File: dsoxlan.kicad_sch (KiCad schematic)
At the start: 6 parts, among them P1 CNT-RJ45, P2 CONN_02X40

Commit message: Basic upgrade to Kicad 7+
Symbols had to be recreated because they were not part of
original dataset.

Footprint library now needs to end in .pretty

Still many DRC warnings, but the basic result ought to be
the same as before now.
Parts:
- C2: footprint Capacitors_SMD:C_0805_HandSoldering -> Capacitor_SMD:C_0805_2012Metric_Pad1.18x1.45mm_HandSolder
- R1, R2, R3: footprint Resistors_SMD:R_0805_HandSoldering -> Resistor_SMD:R_0805_2012Metric_Pad1.20x1.40mm_HandSolder
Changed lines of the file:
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@@
       (effects (font (size 1.016 1.016)))
     )
-    (property "Footprint" "Resistors_SMD:R_0805_HandSoldering" (at 109.22 96.012 90)
+    (property "Footprint" "Resistor_SMD:R_0805_2012Metric_Pad1.20x1.40mm_HandSolder" (at 109.22 96.012 90)
       (effects (font (size 1.27 1.27)) hide)
     )
@@
       (effects (font (size 1.016 1.016)))
     )
-    (property "Footprint" "Resistors_SMD:R_0805_HandSoldering" (at 109.22 88.392 90)
+    (property "Footprint" "Resistor_SMD:R_0805_2012Metric_Pad1.20x1.40mm_HandSolder" (at 109.22 88.392 90)
       (effects (font (size 1.27 1.27)) hide)
     )
@@
       (effects (font (size 1.016 1.016)) (justify left))
     )
-    (property "Footprint" "Capacitors_SMD:C_0805_HandSoldering" (at 110.1852 71.12 0)
+    (property "Footprint" "Capacitor_SMD:C_0805_2012Metric_Pad1.18x1.45mm_HandSolder" (at 110.1852 71.12 0)
       (effects (font (size 1.27 1.27)) hide)
     )
@@
       (effects (font (size 1.016 1.016)))
     )
-    (property "Footprint" "Resistors_SMD:R_0805_HandSoldering" (at 118.11 71.882 90)
+    (property "Footprint" "Resistor_SMD:R_0805_2012Metric_Pad1.20x1.40mm_HandSolder" (at 118.11 71.882 90)
       (effects (font (size 1.27 1.27)) hide)
     )

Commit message: DSC fixup
Replace all objects by new ones from the current libraries
shipped by Kicad.

This causes a slightly different OSHW (Opensource Hardware)
logo to be used in the PCB.

To maintain schematic parity, all mechanical objects on the
PCB (mounting holes and OSHW logo) have their schematic
counterparts now.
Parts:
- added H101, H102, H103, H104: MountingHole, MountingHole:MountingHole_3.2mm_M3_ISO7380, symbol Mechanical:MountingHole
- added SYM101: Logo_Open_Hardware_Small, Symbol:OSHW-Symbol_6.7x6mm_Copper, symbol Graphic:Logo_Open_Hardware_Small
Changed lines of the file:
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@@
+    )
+  )
+  (symbol (lib_id "Mechanical:MountingHole") (at 83.82 139.7 0) (unit 1)
+    (in_bom yes) (on_board yes) (dnp no) (fields_autoplaced)
+    (property "Reference" "H101" (at 86.36 139.0563 0)
+      (effects (font (size 1.27 1.27)) (justify left))
+    )
+    (property "Value" "MountingHole" (at 86.36 140.9773 0)
+      (effects (font (size 1.27 1.27)) (justify left))
+    )
+    (property "Footprint" "MountingHole:MountingHole_3.2mm_M3_ISO7380" (at 83.82 139.7 0)
+      (effects (font (size 1.27 1.27)) hide)
+    )
+    (property "Datasheet" "~" (at 83.82 139.7 0)
+      (effects (font (size 1.27 1.27)) hide)
+    )
+    (instances
+      (project "dsoxlan"
+        (path "/071cacbe-efce-4cc8-8d6c-a55997c1e3c5"
+          (reference "H101") (unit 1)
+        )
+      )
+    )
+  )
+  (symbol (lib_id "Mechanical:MountingHole") (at 83.82 158.75 0) (unit 1)
+    (in_bom yes) (on_board yes) (dnp no) (fields_autoplaced)
+    (property "Reference" "H104" (at 86.36 158.1063 0)
+      (effects (font (size 1.27 1.27)) (justify left))
+    )
+    (property "Value" "MountingHole" (at 86.36 160.0273 0)
+      (effects (font (size 1.27 1.27)) (justify left))
+    )
+    (property "Footprint" "MountingHole:MountingHole_3.2mm_M3_ISO7380" (at 83.82 158.75 0)
+      (effects (font (size 1.27 1.27)) hide)
+    )
+    (property "Datasheet" "~" (at 83.82 158.75 0)
+      (effects (font (size 1.27 1.27)) hide)
+    )
+    (instances
+      (project "dsoxlan"
+        (path "/071cacbe-efce-4cc8-8d6c-a55997c1e3c5"
+          (reference "H104") (unit 1)
+        )
+      )
+    )
+  )
+  (symbol (lib_id "Mechanical:MountingHole") (at 83.82 146.05 0) (unit 1)
+    (in_bom yes) (on_board yes) (dnp no) (fields_autoplaced)
+    (property "Reference" "H102" (at 86.36 145.4063 0)
+      (effects (font (size 1.27 1.27)) (justify left))
+    )
+    (property "Value" "MountingHole" (at 86.36 147.3273 0)
+      (effects (font (size 1.27 1.27)) (justify left))
+    )
+    (property "Footprint" "MountingHole:MountingHole_3.2mm_M3_ISO7380" (at 83.82 146.05 0)
+      (effects (font (size 1.27 1.27)) hide)
+    )
+    (property "Datasheet" "~" (at 83.82 146.05 0)
+      (effects (font (size 1.27 1.27)) hide)
+    )
+    (instances
+      (project "dsoxlan"
+        (path "/071cacbe-efce-4cc8-8d6c-a55997c1e3c5"
+          (reference "H102") (unit 1)
+        )
+      )
+    )
+  )
+  (symbol (lib_id "Graphic:Logo_Open_Hardware_Small") (at 86.36 175.26 0) (unit 1)
+    (in_bom no) (on_board yes) (dnp no) (fields_autoplaced)
+    (property "Reference" "SYM101" (at 86.36 168.275 0)
+      (effects (font (size 1.27 1.27)) hide)
+    )
+    (property "Value" "Logo_Open_Hardware_Small" (at 86.36 180.975 0)
+      (effects (font (size 1.27 1.27)) hide)
+    )
+    (property "Footprint" "Symbol:OSHW-Symbol_6.7x6mm_Copper" (at 86.36 175.26 0)
+      (effects (font (size 1.27 1.27)) hide)
+    )
+    (property "Datasheet" "~" (at 86.36 175.26 0)
+      (effects (font (size 1.27 1.27)) hide)
+    )
+    (property "Sim.Enable" "0" (at 86.36 175.26 0)
+      (effects (font (size 1.27 1.27)) hide)
+    )
+    (instances
+      (project "dsoxlan"
+        (path "/071cacbe-efce-4cc8-8d6c-a55997c1e3c5"
+          (reference "SYM101") (unit 1)
+        )
+      )
+    )
+  )
+  (symbol (lib_id "Mechanical:MountingHole") (at 83.82 152.4 0) (unit 1)
+    (in_bom yes) (on_board yes) (dnp no) (fields_autoplaced)
+    (property "Reference" "H103" (at 86.36 151.7563 0)
+      (effects (font (size 1.27 1.27)) (justify left))
+    )
+    (property "Value" "MountingHole" (at 86.36 153.6773 0)
+      (effects (font (size 1.27 1.27)) (justify left))
+    )
+    (property "Footprint" "MountingHole:MountingHole_3.2mm_M3_ISO7380" (at 83.82 152.4 0)
+      (effects (font (size 1.27 1.27)) hide)
+    )
+    (property "Datasheet" "~" (at 83.82 152.4 0)
+      (effects (font (size 1.27 1.27)) hide)
+    )
+    (instances
+      (project "dsoxlan"
+        (path "/071cacbe-efce-4cc8-8d6c-a55997c1e3c5"
+          (reference "H103") (unit 1)
+        )
+      )
     )
   )

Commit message: Replace RJ45 jack by Bel Fuse 08B0-1X1T-36-F
The old TE Connectivity device is no longer available.

Found another one that contains similar magnetics and
termination as the TE one.
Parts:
- removed P1: CNT-RJ45, DSOXLAN:ETH-MAGJACK, symbol dsoxlan:CNT-RJ45
- added P1: 08B0-1X1T-36-F, DSOXLAN:08B0-1X1T-36-F, symbol dsoxlan:RJ45-BELFUSE
- R1, R2: value 220R -> 470R
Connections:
- net GND: now also P1.13 (Shield), P1.14 (Shield)
- net LED1: now also P1.7 (D1)
- net LED2: now also P1.9 (D3)
- net RX+: now also P1.2
- net RX-: now also P1.3
- net TX+: now also P1.4
- net TX-: now also P1.5
- net at R1.2: now also P1.8 (D2)
- net at R2.2: now also P1.10 (D4)
- net at C2.2, R3.2: now also P1.1, P1.6
- no-connect marks 67 -> 66
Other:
- note added: "AW 2014-12-18, DL8DTL 2024-05-18"
- note removed: "AW 2014-12-18"
- note removed: "Digi-Key 1419-1021-ND"
- moved on the sheet: R1, R2

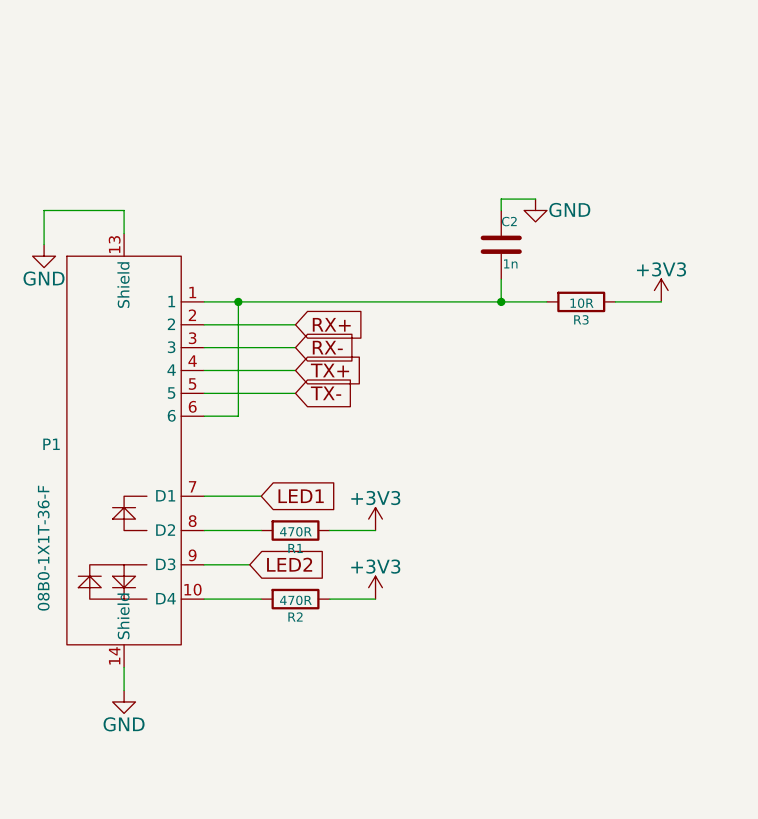
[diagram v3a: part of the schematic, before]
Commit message: Replace RJ45 jack by Würth 7499010121A
This one appears to be readily available at various distributors.

Also add 3D print models for case parts, obtained from

https://www.eevblog.com/forum/projects/diy-dsoxlan-interface-for-keysight-oscilloscopes/msg4323214/#msg4323214

apparently authored by Jay_Diddy_B.

Adapted layout to fit these models.
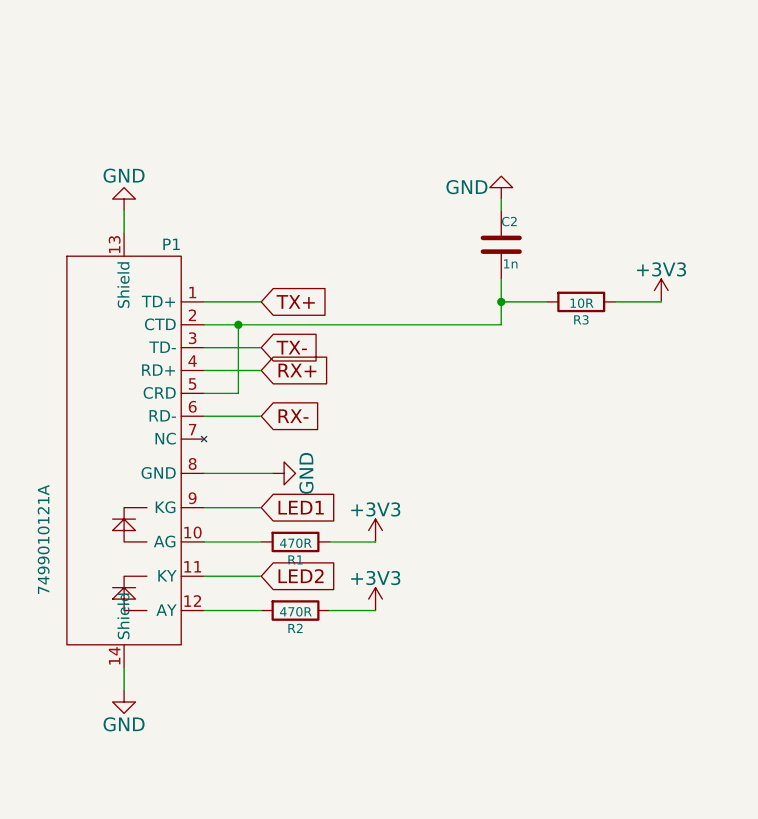
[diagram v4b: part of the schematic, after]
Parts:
- P1: value 08B0-1X1T-36-F -> 7499010121A; footprint DSOXLAN:08B0-1X1T-36-F -> DSOXLAN:WURTH-7499010121A; symbol dsoxlan:RJ45-BELFUSE -> dsoxlan:WÜRTH-7499010121A
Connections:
- net GND: now also P1.8 (GND)
- net LED1: now also P1.9 (KG); no longer P1.7 (D1)
- net LED2: now also P1.11 (KY); no longer P1.9 (D3)
- net RX+: now also P1.4 (RD+); no longer P1.2
- net RX-: now also P1.6 (RD-); no longer P1.3
- net TX+: now also P1.1 (TD+); no longer P1.4
- net TX-: now also P1.3 (TD-); no longer P1.5
- net at R2.2: now also P1.12 (AY); no longer P1.10 (D4)
- net at R1.2: now also P1.10 (AG); no longer P1.8 (D2)
- net at C2.2, R3.2: now also P1.2 (CTD), P1.5 (CRD); no longer P1.1, P1.6
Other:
- moved on the sheet: R1, R2

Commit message: update to kicad9
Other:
- title: (none) -> DSOXLAN
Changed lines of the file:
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@@
 (kicad_sch
-	(version 20231120)
+	(version 20250114)
 	(generator "eeschema")
-	(generator_version "8.0")
+	(generator_version "9.0")
 	(paper "A4")
+	(title_block
+		(title "DSOXLAN")
+	)
+	(text "bottom-side"
+		(exclude_from_sim no)
+		(at 201.93 138.43 0)
+		(effects
+			(font
+				(size 1.524 1.524)
+			)
+			(justify left bottom)
+		)
+	)
+	(text "top-side"
+		(exclude_from_sim no)
+		(at 170.18 34.29 0)
+		(effects
+			(font
+				(size 1.524 1.524)
+			)
+			(justify left bottom)
+		)
+	)
+	(text "left edge of card"
+		(exclude_from_sim no)
+		(at 179.07 139.7 0)
+		(effects
+			(font
+				(size 1.524 1.524)
+			)
+			(justify left bottom)
+		)
+	)
+	(text "DIY DSOXLAN for Agilent DSO-X 2000 and 3000"
+		(exclude_from_sim no)
+		(at 193.04 173.99 0)
+		(effects
+			(font
+				(size 1.524 1.524)
+			)
+			(justify left bottom)
+		)
+	)
+	(text "AW 2014-12-18, DL8DTL 2024-05-18"
+		(exclude_from_sim no)
+		(at 193.04 179.07 0)
+		(effects
+			(font
+				(size 1.524 1.524)
+			)
+			(justify left bottom)
+		)
+	)
+	(text "right edge of card"
+		(exclude_from_sim no)
+		(at 177.8 30.48 0)
+		(effects
+			(font
+				(size 1.524 1.524)
+			)
+			(justify left bottom)
+		)
+	)
+	(text "top-side"
+		(exclude_from_sim no)
+		(at 167.64 137.16 0)
+		(effects
+			(font
+				(size 1.524 1.524)
+			)
+			(justify left bottom)
+		)
+	)
+	(text "bottom-side"
+		(exclude_from_sim no)
+		(at 198.12 34.29 0)
+		(effects
+			(font
+				(size 1.524 1.524)
+			)
+			(justify left bottom)
+		)
+	)
+	(text "notch in card-edge connector"
+		(exclude_from_sim no)
+		(at 200.66 90.17 0)
+		(effects
+			(font
+				(size 1.524 1.524)
+			)
+			(justify left bottom)
+		)
+	)
+	(text "LAN_EN"
+		(exclude_from_sim no)
+		(at 200.66 134.62 0)
+		(effects
+			(font
+				(size 1.524 1.524)
+			)
+			(justify left bottom)
+		)
+	)
 	(junction
 		(at 204.47 101.6)
@@
 			(width 0)
 			(type default)
-		)
-	)
-	(text "bottom-side"
-		(exclude_from_sim no)
-		(at 201.93 138.43 0)
-		(effects
-			(font
-				(size 1.524 1.524)
-			)
-			(justify left bottom)
-		)
-	)
-	(text "top-side"
-		(exclude_from_sim no)
-		(at 170.18 34.29 0)
-		(effects
-			(font
-				(size 1.524 1.524)
-			)
-			(justify left bottom)
-		)
-	)
-	(text "left edge of card"
-		(exclude_from_sim no)
-		(at 179.07 139.7 0)
-		(effects
-			(font
-				(size 1.524 1.524)
-			)
-			(justify left bottom)
-		)
-	)
-	(text "DIY DSOXLAN for Agilent DSO-X 2000 and 3000"
-		(exclude_from_sim no)
-		(at 193.04 173.99 0)
-		(effects
-			(font
-				(size 1.524 1.524)
-			)
-			(justify left bottom)
-		)
-	)
-	(text "AW 2014-12-18, DL8DTL 2024-05-18"
-		(exclude_from_sim no)
-		(at 193.04 179.07 0)
-		(effects
-			(font
-				(size 1.524 1.524)
-			)
-			(justify left bottom)
-		)
-	)
-	(text "right edge of card"
-		(exclude_from_sim no)
-		(at 177.8 30.48 0)
-		(effects
-			(font
-				(size 1.524 1.524)
-			)
-			(justify left bottom)
-		)
-	)
-	(text "top-side"
-		(exclude_from_sim no)
-		(at 167.64 137.16 0)
-		(effects
-			(font
-				(size 1.524 1.524)
-			)
-			(justify left bottom)
-		)
-	)
-	(text "bottom-side"
-		(exclude_from_sim no)
-		(at 198.12 34.29 0)
-		(effects
-			(font
-				(size 1.524 1.524)
-			)
-			(justify left bottom)
-		)
-	)
-	(text "notch in card-edge connector"
-		(exclude_from_sim no)
-		(at 200.66 90.17 0)
-		(effects
-			(font
-				(size 1.524 1.524)
-			)
-			(justify left bottom)
-		)
-	)
-	(text "LAN_EN"
-		(exclude_from_sim no)
-		(at 200.66 134.62 0)
-		(effects
-			(font
-				(size 1.524 1.524)
-			)
-			(justify left bottom)
 		)
 	)
@@
 		)
 	)
+	(embedded_fonts no)
 )
